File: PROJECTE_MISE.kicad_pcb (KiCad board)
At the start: 2 copper layers, 75 x 80 mm, 46 parts, among them IC1 MSP430FR2355TPT, J1 conn_DFrobot, J10 SDA_{TP}, J11 SCL_{TP}, J12 SCL_{TP-GND}, J13 SPI_{TP-MISO}, J14 SPI_{TP-SS}, J15 SPI_{TP-SCLK}, J16 SPI_{TP-MOSI}, J17 SPI_{TP-GND}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

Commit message: layout better
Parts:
- moved R4 81.9 mm to (107.0, 64.9)
- moved R5 81.1 mm to (102.0, 64.9)
- moved C3 76.2 mm to (115.5, 65.5)
- moved J15 71.1 mm to (121.5, 113.0)
- moved J17 70.6 mm to (121.5, 118.0)
- moved J16 65.3 mm to (126.5, 113.0)
- moved J14 64.9 mm to (125.5, 122.0)
- moved J13 63.9 mm to (126.0, 118.0)
- moved J5 59.5 mm to (131.0, 118.5)
- moved J4 57.9 mm to (131.0, 113.0)
- moved J11 56.6 mm to (136.0, 113.0)
- moved J9 46.2 mm to (141.5, 119.0)
- moved J10 44.3 mm to (141.0, 113.0)
- moved J12 42.2 mm to (136.5, 119.0)
- moved C5 28.7 mm to (76.5, 126.0)
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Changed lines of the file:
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@@
 	(footprint "Connector_PinSocket_2.54mm:PinSocket_2x04_P2.54mm_Vertical"
 		(layer "F.Cu")
-		(at 130.96 77.58 180)
+		(at 128 77.62 180)
 		(descr "Through hole straight socket strip, 2x04, 2.54mm pitch, double cols (from Kicad 4.0.7), script generated")
 		(tags "Through hole socket strip THT 2x04 2.54mm double row")
@@
 	(footprint "Connector_PinHeader_1.00mm:PinHeader_1x01_P1.00mm_Vertical"
 		(layer "F.Cu")
-		(at 182.31 76.12)
+		(at 121.5 113)
 		(descr "Through hole straight pin header, 1x01, 1.00mm pitch, single row")
 		(tags "Through hole pin header THT 1x01 1.00mm single row")
@@
 	(footprint "Connector_PinHeader_1.00mm:PinHeader_1x01_P1.00mm_Vertical"
 		(layer "F.Cu")
-		(at 171 83.5)
+		(at 141.5 119)
 		(descr "Through hole straight pin header, 1x01, 1.00mm pitch, single row")
 		(tags "Through hole pin header THT 1x01 1.00mm single row")
@@
 		)
 		(property "Value" "conn_DFrobot"
-			(at -5.52 0.5 360)
+			(at -5.52 0.5 0)
 			(layer "F.Fab")
 			(effects
@@
 	(footprint "Resistor_SMD:R_0805_2012Metric"
 		(layer "F.Cu")
-		(at 77.27 141.19 -90)
+		(at 107 64.9125 -90)
 		(descr "Resistor SMD 0805 (2012 Metric), square (rectangular) end terminal, IPC_7351 nominal, (Body size source: IPC-SM-782 page 72, https://www.pcb-3d.com/wordpress/wp-content/uploads/ipc-sm-782a_amendment_1_and_2.pdf), generated with kicad-footprint-generator")
 		(tags "resistor")
@@
 	(footprint "Package_TO_SOT_THT:TO-92_Inline"
 		(layer "F.Cu")
-		(at 139.23 74.86)
+		(at 140.14 75.73 -90)
 		(descr "TO-92 leads in-line, narrow, oval pads, drill 0.75mm (see NXP sot054_po.pdf)")
 		(tags "to-92 sc-43 sc-43a sot54 PA33 transistor")
 		(property "Reference" "Q1"
-			(at 1.27 -3.56 0)
+			(at 1.27 -3.56 90)
 			(layer "F.SilkS")
 			(effects
@@
 		)
 		(property "Value" "BC547"
-			(at 1.27 2.79 0)
+			(at 1.27 2.79 90)
 			(layer "F.Fab")
 			(effects
@@
 		)
 		(property "Footprint" "Package_TO_SOT_THT:TO-92_Inline"
-			(at 0 0 0)
+			(at 0 0 -90)
 			(unlocked yes)
 			(layer "F.Fab")
@@
 		)
 		(property "Datasheet" "https://www.onsemi.com/pub/Collateral/BC550-D.pdf"
-			(at 0 0 0)
+			(at 0 0 -90)
 			(unlocked yes)
 			(layer "F.Fab")
@@
 		)
 		(property "Description" "0.1A Ic, 45V Vce, Small Signal NPN Transistor, TO-92"
-			(at 0 0 0)
+			(at 0 0 -90)
 			(unlocked yes)
 			(layer "F.Fab")
@@
 		)
 		(fp_line
-			(start -1.46 -2.73)
+			(start 4 2.01)
 			(end -1.46 2.01)
 			(stroke
@@
 		)
 		(fp_line
-			(start -1.46 -2.73)
+			(start 4 2.01)
 			(end 4 -2.73)
 			(stroke
@@
 		)
 		(fp_line
-			(start 4 2.01)
+			(start -1.46 -2.73)
 			(end -1.46 2.01)
 			(stroke
@@
 		)
 		(fp_line
-			(start 4 2.01)
+			(start -1.46 -2.73)
 			(end 4 -2.73)
 			(stroke
@@
 		)
 		(fp_text user "${REFERENCE}"
-			(at 1.27 0 0)
+			(at 1.27 0 90)
 			(layer "F.Fab")
 			(effects
@@
 		)
 		(pad "1" thru_hole rect
-			(at 0 0)
+			(at 0 0 270)
 			(size 1.05 1.5)
 			(drill 0.75)
@@
 		)
 		(pad "2" thru_hole oval
-			(at 1.27 0)
+			(at 1.27 0 270)
 			(size 1.05 1.5)
 			(drill 0.75)
@@
 		)
 		(pad "3" thru_hole oval
-			(at 2.54 0)
+			(at 2.54 0 270)
 			(size 1.05 1.5)
 			(drill 0.75)
@@
 	(footprint "Resistor_SMD:R_0805_2012Metric"
 		(layer "F.Cu")
-		(at 74.32 141.19 -90)
+		(at 102 64.9125 -90)
 		(descr "Resistor SMD 0805 (2012 Metric), square (rectangular) end terminal, IPC_7351 nominal, (Body size source: IPC-SM-782 page 72, https://www.pcb-3d.com/wordpress/wp-content/uploads/ipc-sm-782a_amendment_1_and_2.pdf), generated with kicad-footprint-generator")
 		(tags "resistor")
@@
 	(footprint "Capacitor_SMD:C_0805_2012Metric"
 		(layer "F.Cu")
-		(at 106.88 141.21 -90)
+		(at 115.5 65.45 -90)
 		(descr "Capacitor SMD 0805 (2012 Metric), square (rectangular) end terminal, IPC_7351 nominal, (Body size source: IPC-SM-782 page 76, https://www.pcb-3d.com/wordpress/wp-content/uploads/ipc-sm-782a_amendment_1_and_2.pdf, https://docs.google.com/spreadsheets/d/1BsfQQcO9C6DZCsRaXUlFlo91Tg2WpOkGARC1WS5S8t0/edit?usp=sharing), generated with kicad-footprint-generator")
 		(tags "capacitor")
@@
 	(footprint "Capacitor_SMD:C_0805_2012Metric"
 		(layer "F.Cu")
-		(at 100.86 141.21 -90)
+		(at 76.5 126.05 -90)
 		(descr "Capacitor SMD 0805 (2012 Metric), square (rectangular) end terminal, IPC_7351 nominal, (Body size source: IPC-SM-782 page 76, https://www.pcb-3d.com/wordpress/wp-content/uploads/ipc-sm-782a_amendment_1_and_2.pdf, https://docs.google.com/spreadsheets/d/1BsfQQcO9C6DZCsRaXUlFlo91Tg2WpOkGARC1WS5S8t0/edit?usp=sharing), generated with kicad-footprint-generator")
 		(tags "capacitor")
@@
 	(footprint "Connector_PinHeader_1.00mm:PinHeader_1x01_P1.00mm_Vertical"
 		(layer "F.Cu")
-		(at 178.96 76.12)
+		(at 136 113)
 		(descr "Through hole straight pin header, 1x01, 1.00mm pitch, single row")
 		(tags "Through hole pin header THT 1x01 1.00mm single row")
@@
 	(footprint "Connector_PinHeader_1.00mm:PinHeader_1x01_P1.00mm_Vertical"
 		(layer "F.Cu")
-		(at 175.61 79.17)
+		(at 131 118.5)
 		(descr "Through hole straight pin header, 1x01, 1.00mm pitch, single row")
 		(tags "Through hole pin header THT 1x01 1.00mm single row")
@@
 	(footprint "Connector_PinHeader_1.00mm:PinHeader_1x01_P1.00mm_Vertical"
 		(layer "F.Cu")
-		(at 150 79)
+		(at 136.5 119)
 		(descr "Through hole straight pin header, 1x01, 1.00mm pitch, single row")
 		(tags "Through hole pin header THT 1x01 1.00mm single row")
@@
 	(footprint "Connector_PinHeader_1.00mm:PinHeader_1x01_P1.00mm_Vertical"
 		(layer "F.Cu")
-		(at 178.96 82.22)
+		(at 126 118)
 		(descr "Through hole straight pin header, 1x01, 1.00mm pitch, single row")
 		(tags "Through hole pin header THT 1x01 1.00mm single row")
@@
 	(footprint "Connector_PinHeader_1.00mm:PinHeader_1x01_P1.00mm_Vertical"
 		(layer "F.Cu")
-		(at 182.31 82.22)
+		(at 121.5 118)
 		(descr "Through hole straight pin header, 1x01, 1.00mm pitch, single row")
 		(tags "Through hole pin header THT 1x01 1.00mm single row")
@@
 	(footprint "Connector_PinHeader_1.00mm:PinHeader_1x01_P1.00mm_Vertical"
 		(layer "F.Cu")
-		(at 175.61 85.27)
+		(at 141 113)
 		(descr "Through hole straight pin header, 1x01, 1.00mm pitch, single row")
 		(tags "Through hole pin header THT 1x01 1.00mm single row")
@@
 	(footprint "Capacitor_SMD:C_0805_2012Metric"
 		(layer "F.Cu")
-		(at 120.5 74 -90)
+		(at 121 65.45 -90)
 		(descr "Capacitor SMD 0805 (2012 Metric), square (rectangular) end terminal, IPC_7351 nominal, (Body size source: IPC-SM-782 page 76, https://www.pcb-3d.com/wordpress/wp-content/uploads/ipc-sm-782a_amendment_1_and_2.pdf, https://docs.google.com/spreadsheets/d/1BsfQQcO9C6DZCsRaXUlFlo91Tg2WpOkGARC1WS5S8t0/edit?usp=sharing), generated with kicad-footprint-generator")
 		(tags "capacitor")
@@
 	(footprint "Connector_PinHeader_1.00mm:PinHeader_1x01_P1.00mm_Vertical"
 		(layer "F.Cu")
-		(at 182.31 79.17)
+		(at 126.5 113)
 		(descr "Through hole straight pin header, 1x01, 1.00mm pitch, single row")
 		(tags "Through hole pin header THT 1x01 1.00mm single row")
@@
 	(footprint "Connector_PinHeader_1.00mm:PinHeader_1x01_P1.00mm_Vertical"
 		(layer "F.Cu")
-		(at 175.61 76.12)
+		(at 131 113)
 		(descr "Through hole straight pin header, 1x01, 1.00mm pitch, single row")
 		(tags "Through hole pin header THT 1x01 1.00mm single row")
@@
 	(footprint "Connector_PinHeader_1.00mm:PinHeader_1x01_P1.00mm_Vertical"
 		(layer "F.Cu")
-		(at 178.96 85.27)
+		(at 125.5 122)
 		(descr "Through hole straight pin header, 1x01, 1.00mm pitch, single row")
 		(tags "Through hole pin header THT 1x01 1.00mm single row")

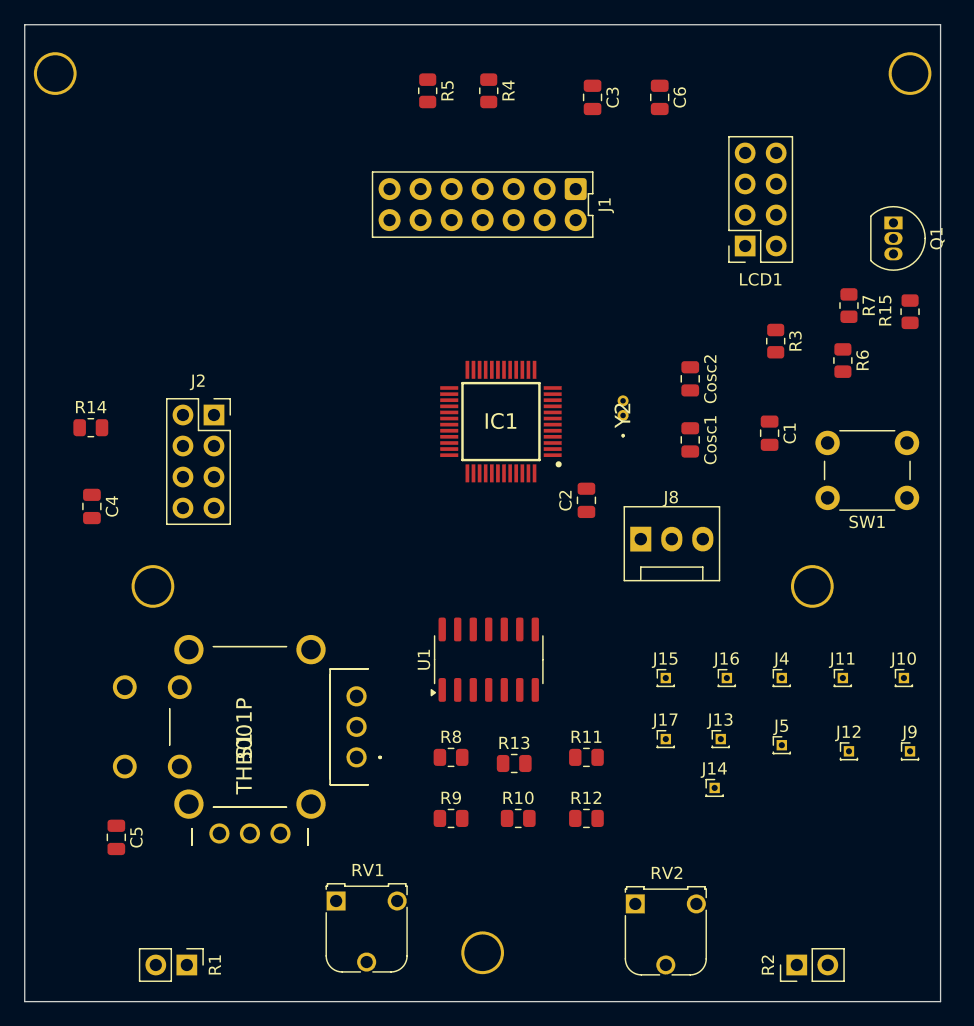
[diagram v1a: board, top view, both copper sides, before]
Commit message: placement i canvi esqu.
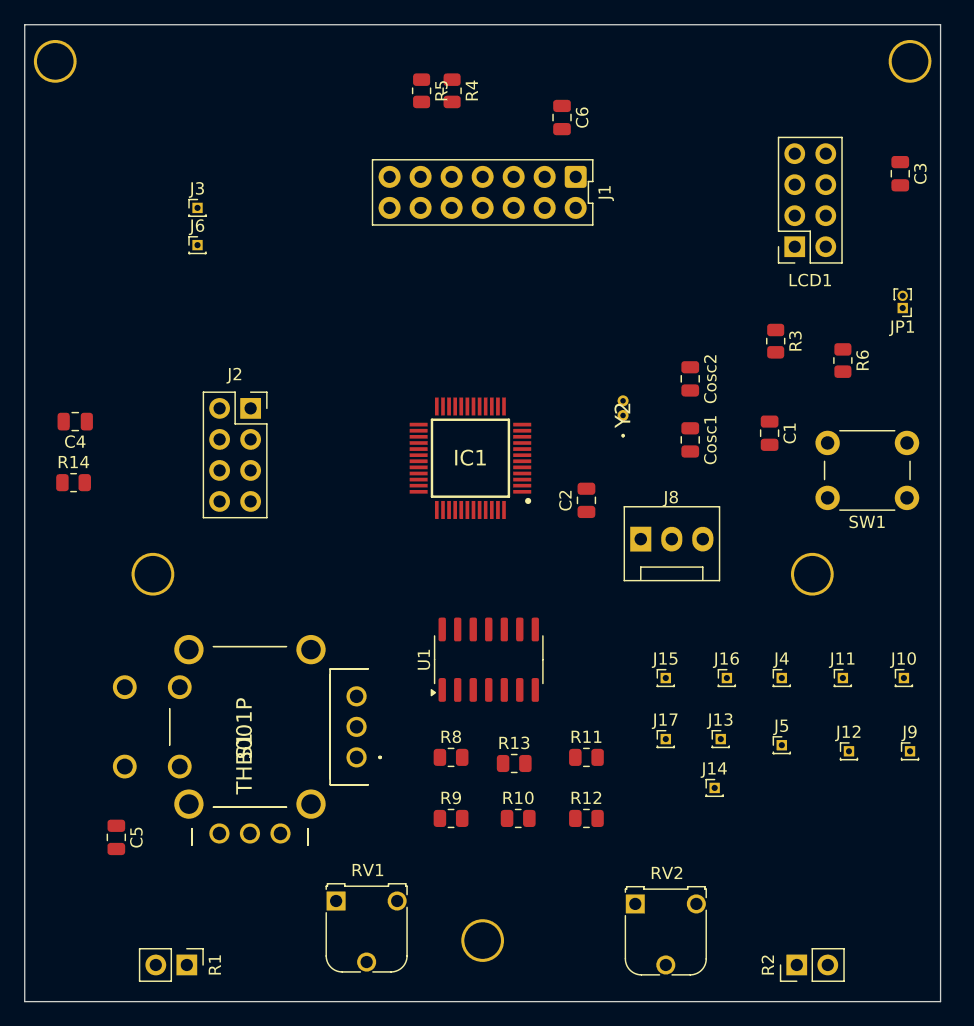
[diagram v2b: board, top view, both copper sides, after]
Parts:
- removed Q1: BC547, Package_TO_SOT_THT:TO-92_Inline
- removed R15: 35K, Resistor_SMD:R_0805_2012Metric
- removed R7: 1K, Resistor_SMD:R_0805_2012Metric
- added J3: Conn_TX_TP, Connector_PinHeader_1.00mm:PinHeader_1x01_P1.00mm_Vertical, F.Cu at (83.2, 74.5)
- added J6: Conn_RX_TP, Connector_PinHeader_1.00mm:PinHeader_1x01_P1.00mm_Vertical, F.Cu at (83.2, 77.5)
- added JP1: Jumper_LCD, Connector_PinHeader_1.00mm:PinHeader_1x02_P1.00mm_Vertical, F.Cu at (140.9, 82.7)
- moved C3 26.0 mm to (140.7, 71.7)
- moved C6 8.17 mm to (113.0, 67.1)
- moved C4 7.08 mm to (73.1, 92.0), turned to 180 degrees
- moved R14 4.72 mm to (73.0, 97.0)
- moved LCD1 4.06 mm to (132.1, 77.7)
- moved IC1 3.91 mm to (105.5, 95.0)
- moved J2 3.05 mm to (87.5, 90.9)
- moved R4 3.00 mm to (104.0, 64.9)
- moved J1 1.00 mm to (106.5, 74.5)
- moved R5 0.50 mm to (101.5, 64.9)
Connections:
- net /RXD_{MSP} renamed /TX_{ESP}
- net Net-(LCD1-K) renamed /K
- IC1 pad 1: /I2C_SDA -> unconnected-(IC1-P1.2/UCB0SIMO/UCB0SDA/TB0TRG/OA0-/A2/VEREF--Pad1)
- IC1 pad 12: /SPI_MISO -> /I2C_SCL
- IC1 pad 13: /SPI_MOSI -> /I2C_SDA
- IC1 pad 19: /P8 -> unconnected-(IC1-P6.3/TB3.4-Pad19)
- IC1 pad 20: /P2 -> /P0
- IC1 pad 22: /P0 -> /P2
- IC1 pad 27: /RST_{ESP} -> unconnected-(IC1-P2.3/TB1TRG-Pad27)
- IC1 pad 41: /BL_EN -> unconnected-(IC1-P5.2/TB2CLK/A10-Pad41)
- IC1 pad 47: /~{RST_{LCD}} -> unconnected-(IC1-P3.0/MCLK-Pad47)
- IC1 pad 48: /I2C_SCL -> unconnected-(IC1-P1.3/UCB0SOMI/UCB0SCL/OA0+/A3-Pad48)
- J1 pad 5: /SPI_MISO -> unconnected-(J1-Pin_5-Pad5)
- J1 pad 7: /SPI_MOSI -> unconnected-(J1-Pin_7-Pad7)
- J10 pad 1: /I2C_SDA -> unconnected-(J10-Pin_1-Pad1)
- J11 pad 1: /I2C_SCL -> unconnected-(J11-Pin_1-Pad1)
- J13 pad 1: /SPI_MISO -> /I2C_SCL
- J16 pad 1: /SPI_MOSI -> /I2C_SDA
- J2 pad 4: /RST_{ESP} -> unconnected-(J2-Pin_4-Pad4)
- LCD1 pad 6: +3V3 -> /A
- R4 pad 2: /I2C_SCL -> /I2C_SDA
- R5 pad 2: /I2C_SDA -> /I2C_SCL
- R6 pad 2: /BL_DRV -> GND

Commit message: layout conn_robot
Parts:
- moved C3 10.1 mm to (134.7, 79.8), turned to 0 degrees
- moved IC1 7.73 mm to (108.3, 87.8)
- moved J2 3.78 mm to (84.4, 88.8)
- moved LCD1 3.31 mm to (132.4, 74.4)
- moved R4 2.60 mm to (101.5, 64.2)
- moved R5 2.57 mm to (104.0, 64.3)
- moved C6 2.00 mm to (114.2, 68.7), turned to 90 degrees
- moved J1 0.21 mm to (106.6, 74.7)
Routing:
- net /I2C_SCL: track 0.00 -> 83.1 mm, vias 0 -> 4
- net /I2C_SDA: track 0.00 -> 59.7 mm, vias 0 -> 3
- net GND: track 0.00 -> 43.0 mm, vias 0 -> 1
- net /SPI_SCLK: track 0.00 -> 36.3 mm, vias 0 -> 3
- net +3V3: track 0.00 -> 20.4 mm
- net /SPI_SS: track 0.00 -> 16.7 mm, vias 0 -> 2
- net /P0: track 0.00 -> 10.6 mm
- net /P1: track 0.00 -> 9.71 mm
- net /P2: track 0.00 -> 8.87 mm
- added copper zone on F.Cu, net +3V3
- added copper zone on B.Cu, net GND

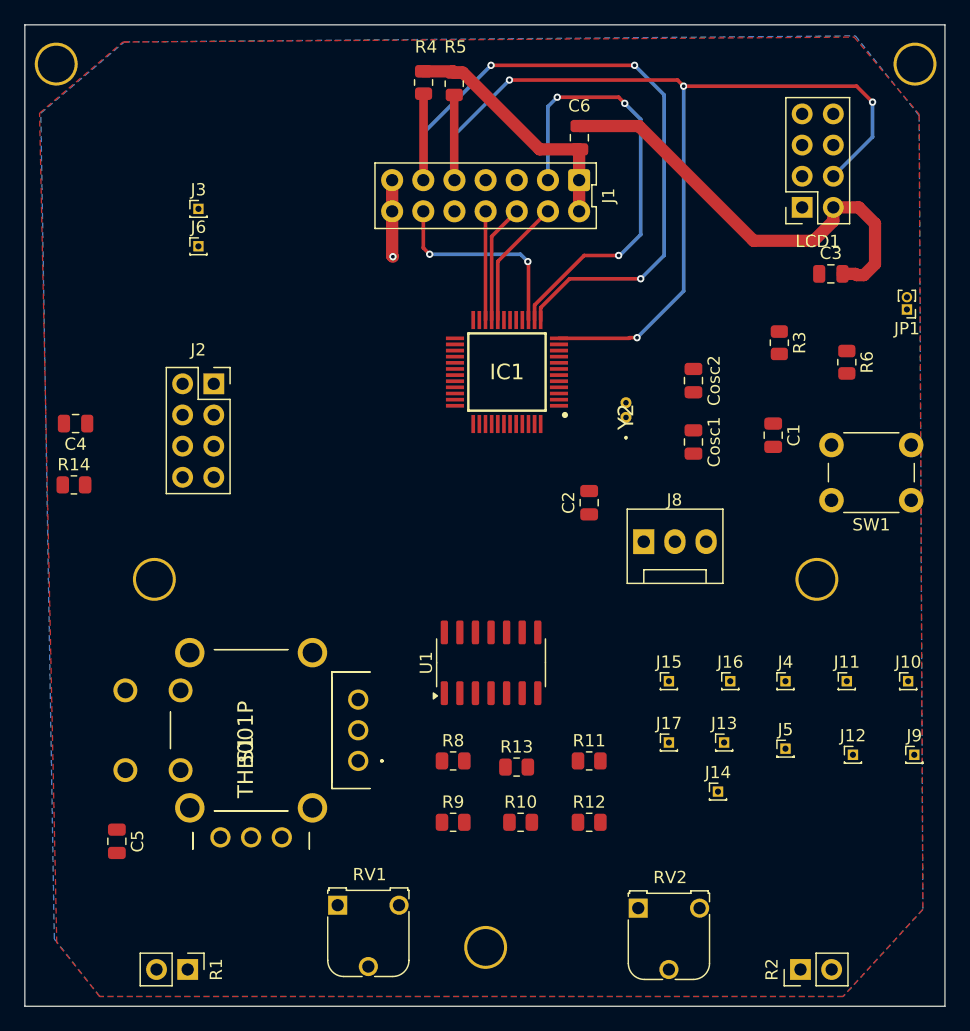
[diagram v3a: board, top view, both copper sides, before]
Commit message: layout with LDRs and better conn
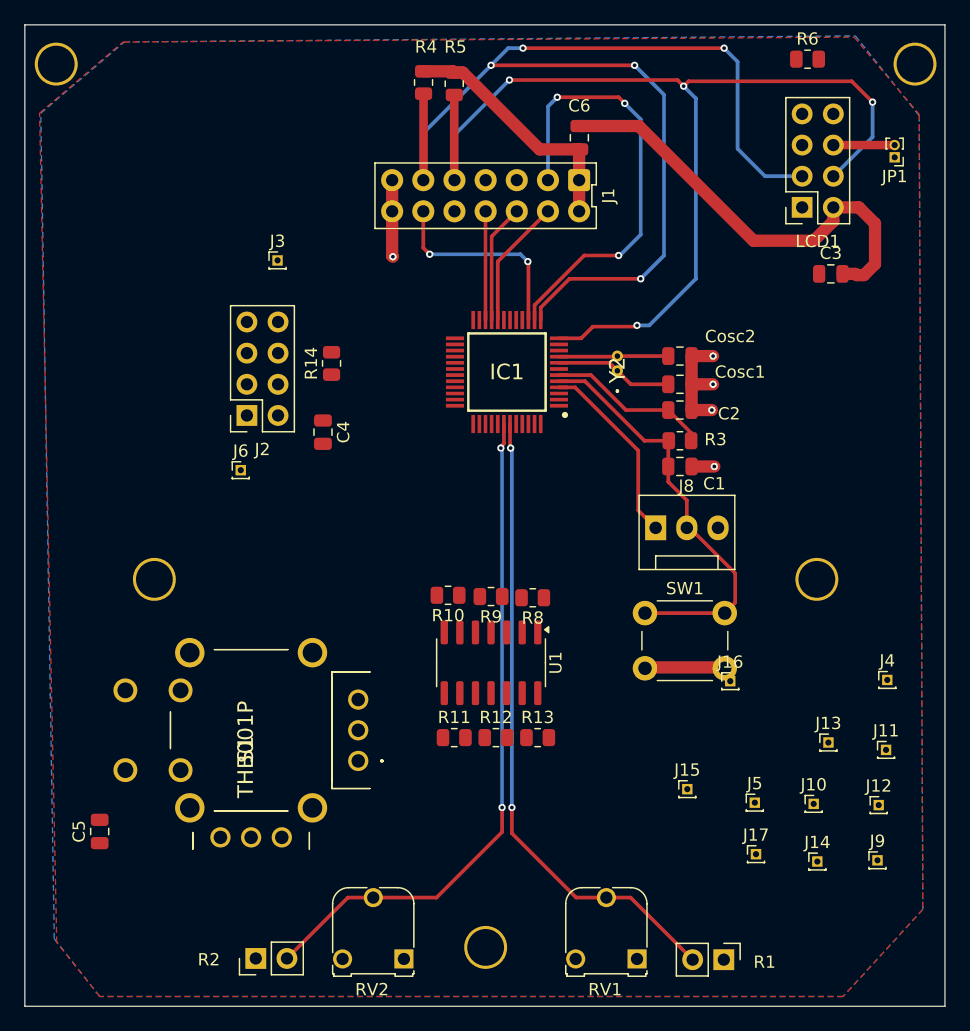
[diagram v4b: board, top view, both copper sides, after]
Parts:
- moved R2 44.4 mm to (87.8, 135.6)
- moved R1 43.7 mm to (126.0, 135.7)
- moved R6 24.9 mm to (132.8, 62.3), turned to 0 degrees
- moved RV1 24.8 mm to (118.9, 135.6), turned to 180 degrees
- moved SW1 23.6 mm to (119.5, 107.5), turned to 0 degrees
- moved R14 23.2 mm to (94.0, 87.1), turned to 90 degrees
- moved C4 20.2 mm to (93.3, 92.7), turned to -90 degrees
- moved RV2 19.5 mm to (99.9, 135.6), turned to 180 degrees
- moved R10 19.4 mm to (103.5, 106.0), turned to 180 degrees
- moved R9 18.7 mm to (107.0, 106.1), turned to 180 degrees
- moved J6 18.6 mm to (86.6, 95.8)
- moved R8 14.8 mm to (110.4, 106.2), turned to 180 degrees
- moved J10 12.6 mm to (133.3, 123.0)
- moved JP1 12.4 mm to (139.9, 70.3)
- moved J17 11.5 mm to (128.6, 127.1)
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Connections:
- IC1 pad 14: /SPI_SCLK -> unconnected-(IC1-P4.5/UCB1CLK-Pad14)
- IC1 pad 15: /SPI_SS -> unconnected-(IC1-P4.4/UCB1STE-Pad15)
- IC1 pad 23: unconnected-(IC1-P4.3/UCA1TXD/UCA1SIMO/~{UCA1TXD}-Pad23) -> /SPI_MOSI
- IC1 pad 24: unconnected-(IC1-P4.2/UCA1RXD/UCA1SOMI/~{UCA1RXD}-Pad24) -> /SPI_MISO
- IC1 pad 25: unconnected-(IC1-P4.1/UCA1CLK-Pad25) -> /SPI_SCLK
- IC1 pad 26: unconnected-(IC1-P4.0/UCA1STE/ISOTXD/ISORXD-Pad26) -> /SPI_SS
- IC1 pad 27: unconnected-(IC1-P2.3/TB1TRG-Pad27) -> /P8
- J1 pad 5: unconnected-(J1-Pin_5-Pad5) -> /SPI_MISO
- J1 pad 7: unconnected-(J1-Pin_7-Pad7) -> /SPI_MOSI
- J10 pad 1: unconnected-(J10-Pin_1-Pad1) -> /I2C_SDA
- J11 pad 1: unconnected-(J11-Pin_1-Pad1) -> /I2C_SCL
- J13 pad 1: /I2C_SCL -> /SPI_MISO
- J16 pad 1: /I2C_SDA -> /SPI_MOSI
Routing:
- net /LDR_{R}: track 0.00 -> 55.2 mm, vias 0 -> 2
- net /LDR_{L}: track 0.00 -> 52.4 mm, vias 0 -> 2
- net /I2C_SDA: track 59.7 -> 94.1 mm, vias 3 -> 5
- net /SBW_{TDIO}: track 0.00 -> 34.3 mm
- net GND: track 43.0 -> 60.9 mm, vias 1 -> 5
- net /SBW_{TCK}: track 0.00 -> 15.5 mm
- net +3V3: track 20.4 -> 33.8 mm
- net /XT1IN: track 0.00 -> 9.64 mm
- net /XT1OUT: track 0.00 -> 8.93 mm
- net /A: track 0.00 -> 5.00 mm
- net /I2C_SCL: track 83.1 -> 84.3 mm
